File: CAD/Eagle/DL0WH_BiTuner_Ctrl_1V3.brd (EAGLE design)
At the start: 96.5 x 73 mm, 157 parts, among them Q0321 ABS07-32.768KHZ, U0101 STM32L476RXT_64PIN_LDO, U0601 MC33996, U0701 MC33996, U0801 MC33996, U0921 TS5A23166, U0941 LM2611, U0951 OPA354, U0961 OPA354, U0962 MCP4661-103E-MS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

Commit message: HW_1V3 - forward until df4fd7a65716eb1a1b8dad1e9e020a2e6c04cd7f (2019-04-03)
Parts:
- removed C0054: 10nF, df4iah_rcl:C0603
- removed R0903, R0913: 150kR, df4iah_rcl:R0402
- removed SJ0401: (no value), df4iah_jumper:SJ
- added C1054: 10nF, df4iah_rcl:C0402
- added R0401: 0R, df4iah_rcl:R0402
- added R0923: 2MR, df4iah_rcl:R0402
- C0942: device df4iah_rcl:C0805 -> df4iah_rcl:C0603
- C1051, C1052, C1053, C1151, C1152, C1153, C1154: device df4iah_rcl:C0603 -> df4iah_rcl:C0402
- R0962: value 1.0kR -> 1kR
- R0972: value 47R -> 1kR
- U0101: value STM32L476RXT_64PIN_LDO -> STM32L476RGT6_64PIN_LDO
- renumbered X0601 to X0501
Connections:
- net +3V3: now also R0401.1; no longer R0903.2, R0913.2, SJ0401.1
- net GND: now also C1054.2, R0923.1; no longer C0054.2
- net MCU_VDD: now also R0401.2; no longer SJ0401.2
- net RS_DTE_RTR: now also C1054.1; no longer C0054.1
- net SWR_IN_FWD: no longer R0903.1
- net SWR_IN_REV: no longer R0913.1
- net SWR_SEL_PWR: now also R0923.2
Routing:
- net +3V3: track 240.7 -> 223.0 mm, vias 11 -> 12
- net SWR_IN_REV: track 4.45 -> 2.53 mm, vias 1 -> 0
- net SWR_SEL_PWR: track 11.0 -> 12.1 mm, vias 1 -> 2
- net SWR_IN_FWD: track 5.94 -> 4.85 mm, vias 1 -> 0
- net GND: vias 38 -> 37
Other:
- board text added: "A"
- board text added: "C"
- board text added: "DL0WH BiTuner Ctrl V1.3 (C) 2019"
- board text removed: "DL0WH BiTuner Ctrl V1.2 (C) 2019"

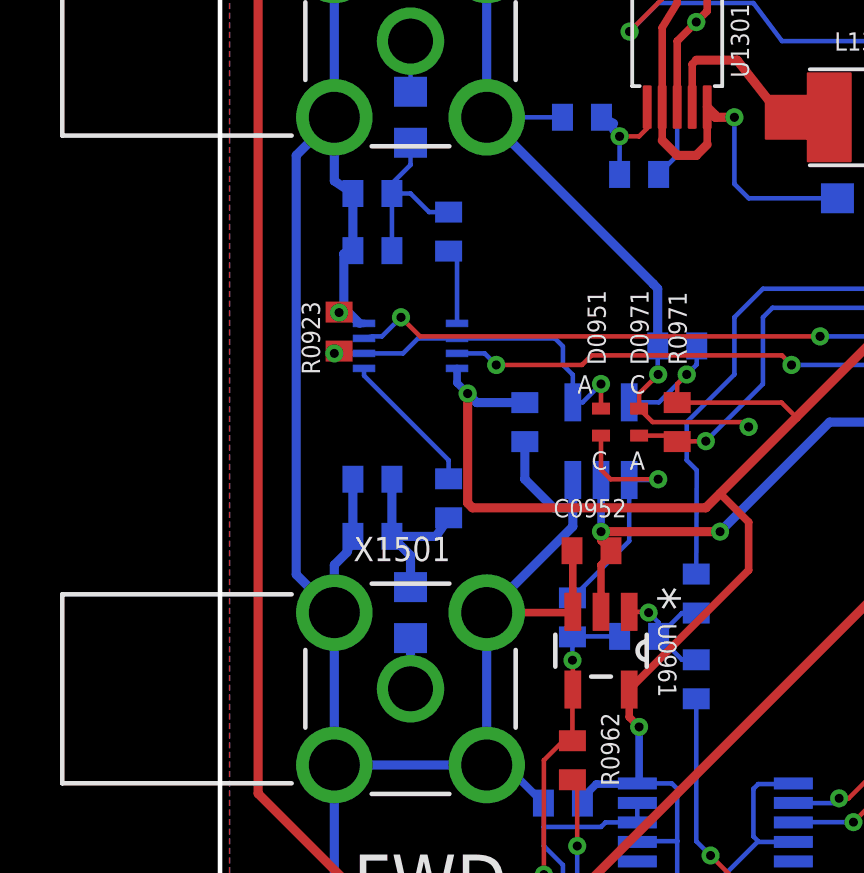
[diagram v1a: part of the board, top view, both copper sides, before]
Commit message: HW_1V2,HW_1V3 - CAD/Eagle - voltage divider added to tolerate voltages 0V..10V
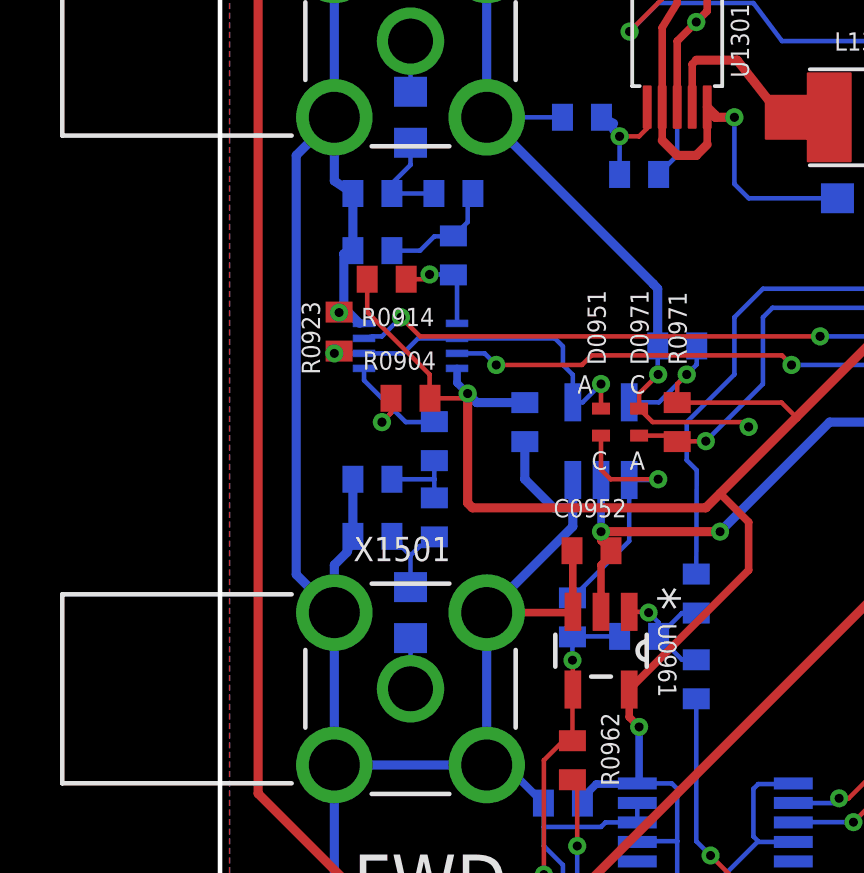
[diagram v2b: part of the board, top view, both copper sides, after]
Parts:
- added R0903, R0913: 15kR, df4iah_rcl:R0402
- added R0904, R0914: 150kR, df4iah_rcl:R0402
- R0901, R0911: value 1kR -> 2kR
- R0902, R0912: value 15kR -> 1kR
- R0963: value 10kR -> 20kR
- moved R0911 3.30 mm to (7.78, 34.3)
- moved R0912 2.62 mm to (5.08, 32.4), turned to 180 degrees
- moved R0902 2.62 mm to (5.08, 24.8), turned to 180 degrees
- moved R0901 2.42 mm to (7.14, 23.5), turned to 90 degrees
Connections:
- new net SWR_IN_FWD_LO: R0901.2, R0902.2, R0903.1
- new net SWR_IN_REV_LO: R0911.2, R0912.2, R0913.1
- net +3V3: now also R0904.2, R0914.2
- net GND: now also R0902.1, R0912.1; no longer R0901.1, R0911.1
- net SWR_IN_FWD: now also R0903.2, R0904.1; no longer R0902.2
- net SWR_IN_FWD_HI: now also R0901.1; no longer R0901.2, R0902.1
- net SWR_IN_REV: now also R0913.2, R0914.1; no longer R0912.2
- net SWR_IN_REV_HI: now also R0911.1; no longer R0911.2, R0912.1
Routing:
- net +3V3: track 223.0 -> 229.1 mm
- net SWR_IN_REV_LO: track 0.00 -> 4.05 mm
- net SWR_IN_FWD_HI: track 6.07 -> 2.99 mm
- net SWR_IN_FWD_LO: track 0.00 -> 2.65 mm
- net SWR_IN_REV_HI: track 6.00 -> 3.35 mm
- net SWR_IN_REV: track 2.53 -> 3.28 mm, vias 0 -> 1
- net SWR_IN_FWD: vias 0 -> 1
